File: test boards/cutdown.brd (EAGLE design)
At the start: 50.8 x 59.7 mm, 12 parts, among them Q1 FDD3706, U1 6N138M

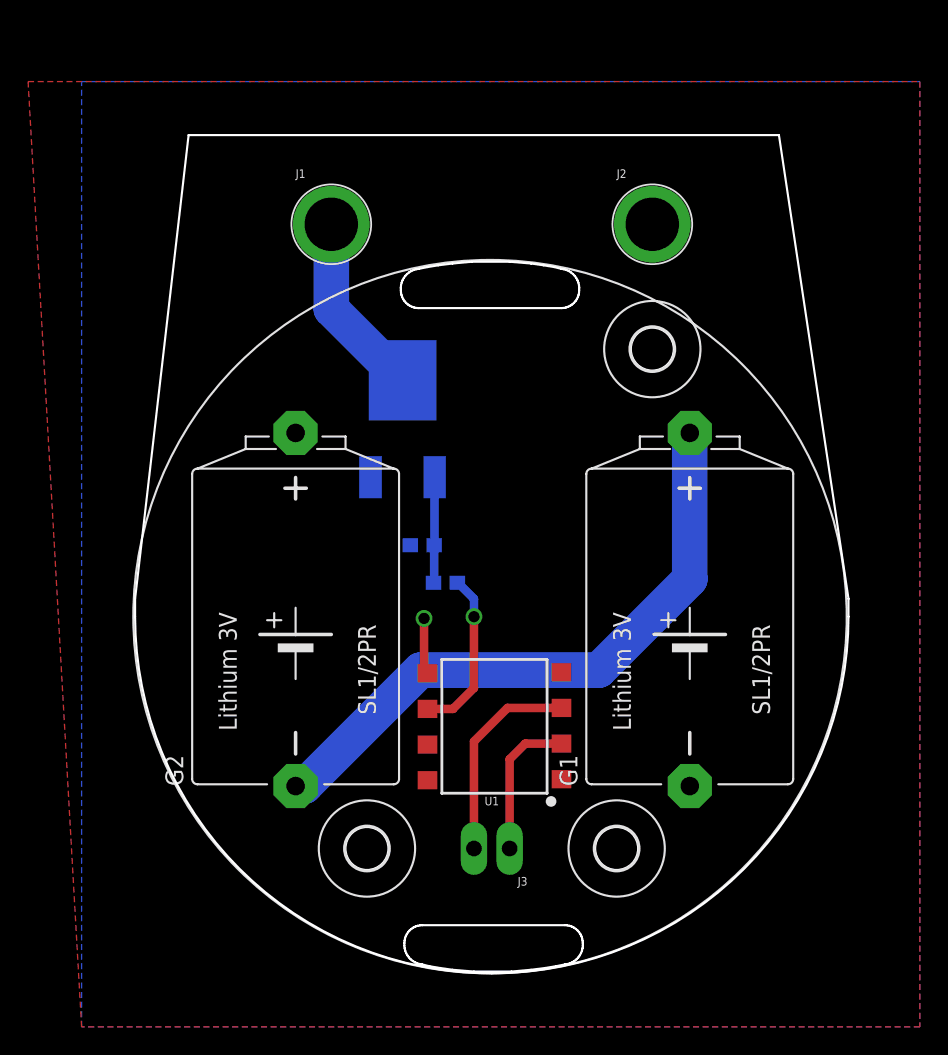
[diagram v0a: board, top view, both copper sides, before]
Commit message: updated board outline
updated board outline to makek the bottom cutout complete.
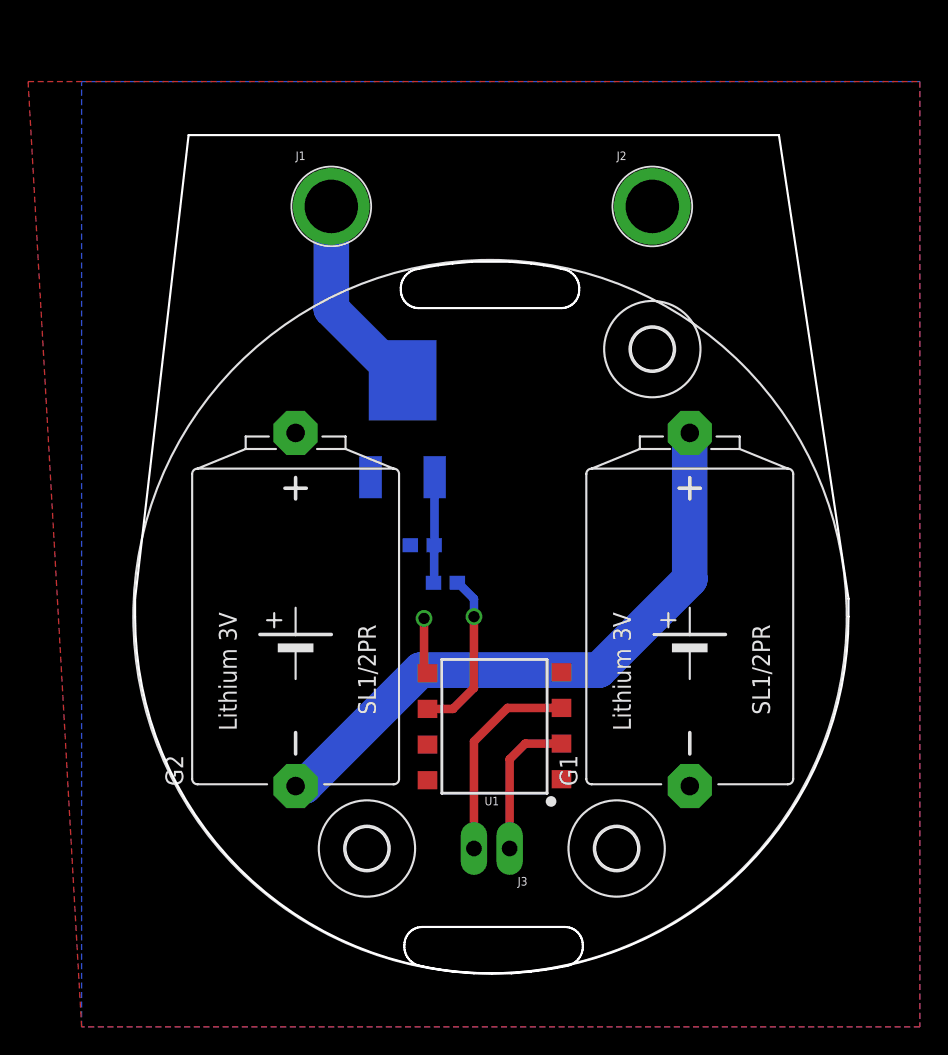
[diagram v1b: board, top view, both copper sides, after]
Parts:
- moved J1 1.27 mm to (31.8, 74.9)
- moved J2 1.27 mm to (54.6, 74.9)
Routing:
- net N$2: track 13.2 -> 14.5 mm
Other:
- outline, holes or cut-outs redrawn
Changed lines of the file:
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@@
 <wire x1="68.58" y1="46.99" x2="63.627" y2="80.01" width="0.1524" layer="20"/>
 <wire x1="17.78" y1="46.99" x2="17.78" y2="45.72" width="0.1524" layer="20"/>
-<wire x1="17.78" y1="45.72" x2="43.18" y2="20.32" width="0.1524" layer="20" curve="90"/>
-<wire x1="43.18" y1="20.32" x2="68.58" y2="45.72" width="0.1524" layer="20" curve="90"/>
+<wire x1="17.78" y1="45.72" x2="43.18" y2="20.32" width="0.1524" layer="20" curve="90" locked="yes"/>
+<wire x1="43.18" y1="20.32" x2="68.58" y2="45.72" width="0.1524" layer="20" curve="90" locked="yes"/>
 <wire x1="68.58" y1="45.72" x2="68.58" y2="46.99" width="0.1524" layer="20"/>
 <polygon width="0.1524" layer="20">
@@
 </polygon>
 <polygon width="0.1524" layer="20">
-<vertex x="49.657" y="22.479" curve="-90"/>
-<vertex x="48.387" y="20.955"/>
-<vertex x="47.752" y="20.828"/>
-<vertex x="46.99" y="20.701"/>
-<vertex x="45.974" y="20.574"/>
-<vertex x="44.577" y="20.447"/>
-<vertex x="41.91" y="20.447"/>
-<vertex x="40.386" y="20.574"/>
-<vertex x="39.497" y="20.701"/>
-<vertex x="38.735" y="20.828"/>
-<vertex x="38.227" y="20.955" curve="-90"/>
-<vertex x="36.957" y="22.479" curve="-90"/>
-<vertex x="38.227" y="23.749"/>
-<vertex x="48.387" y="23.749" curve="-90"/>
+<vertex x="49.657" y="22.352" curve="-90"/>
+<vertex x="48.387" y="20.828"/>
+<vertex x="47.752" y="20.701"/>
+<vertex x="46.99" y="20.574"/>
+<vertex x="45.974" y="20.447"/>
+<vertex x="44.577" y="20.32"/>
+<vertex x="41.91" y="20.32"/>
+<vertex x="40.386" y="20.447"/>
+<vertex x="39.497" y="20.574"/>
+<vertex x="38.735" y="20.701"/>
+<vertex x="38.227" y="20.828" curve="-90"/>
+<vertex x="36.957" y="22.352" curve="-90"/>
+<vertex x="38.227" y="23.622"/>
+<vertex x="48.387" y="23.622" curve="-90"/>
 </polygon>
 <circle x="43.053" y="45.72" radius="25.4" width="0.1524" layer="25"/>
@@
 </class>
 </classes>
-<designrules name="default">
-<description language="de">&lt;b&gt;EAGLE Design Rules&lt;/b&gt;
-&lt;p&gt;
-Die Standard-Design-Rules sind so gewählt, dass sie für
-die meisten Anwendungen passen. Sollte ihre Platine
-besondere Anforderungen haben, treffen Sie die erforderlichen
-Einstellungen hier und speichern die Design Rules unter
-einem neuen Namen ab.</description>
-<description language="en">&lt;b&gt;EAGLE Design Rules&lt;/b&gt;
-&lt;p&gt;
-The default Design Rules have been set to cover
-a wide range of applications. Your particular design
-may have different requirements, so please make the
-necessary adjustments and save your customized
-design rules under a new name.</description>
+<designrules name="MF_Standard_2_Layer">
+<description language="en">&lt;b&gt;MacroFab, INC. EAGLE Design Rules&lt;/b&gt;
+&lt;p&gt;This DRC check is for 2-Layer Standard Capability boards to be manufactured through the MacroFab, INC. service.</description>
 <param name="layerSetup" value="(1*16)"/>
-<param name="mtCopper" value="0.035mm 0.035mm 0.035mm 0.035mm 0.035mm 0.035mm 0.035mm 0.035mm 0.035mm 0.035mm 0.035mm 0.035mm 0.035mm 0.035mm 0.035mm 0.035mm"/>
-<param name="mtIsolate" value="1.5mm 0.15mm 0.2mm 0.15mm 0.2mm 0.15mm 0.2mm 0.15mm 0.2mm 0.15mm 0.2mm 0.15mm 0.2mm 0.15mm 0.2mm"/>
-<param name="mdWireWire" value="6mil"/>
-<param name="mdWirePad" value="6mil"/>
-<param name="mdWireVia" value="6mil"/>
-<param name="mdPadPad" value="6mil"/>
-<param name="mdPadVia" value="6mil"/>
-<param name="mdViaVia" value="6mil"/>
-<param name="mdSmdPad" value="6mil"/>
-<param name="mdSmdVia" value="6mil"/>
-<param name="mdSmdSmd" value="6mil"/>
-<param name="mdViaViaSameLayer" value="6mil"/>
+<param name="mtCopper" value="0.035mm 0.0175mm 0.035mm 0.035mm 0.035mm 0.035mm 0.035mm 0.035mm 0.035mm 0.035mm 0.035mm 0.035mm 0.035mm 0.035mm 0.0175mm 0.035mm"/>
+<param name="mtIsolate" value="1.5mm 1.1mm 0.2mm 0.15mm 0.2mm 0.15mm 0.2mm 0.15mm 0.2mm 0.15mm 0.2mm 0.15mm 0.2mm 0.15mm 0.2mm"/>
+<param name="mdWireWire" value="5mil"/>
+<param name="mdWirePad" value="5mil"/>
+<param name="mdWireVia" value="5mil"/>
+<param name="mdPadPad" value="5mil"/>
+<param name="mdPadVia" value="5mil"/>
+<param name="mdViaVia" value="5mil"/>
+<param name="mdSmdPad" value="0mil"/>
+<param name="mdSmdVia" value="0mil"/>
+<param name="mdSmdSmd" value="0mil"/>
+<param name="mdViaViaSameLayer" value="8mil"/>
 <param name="mnLayersViaInSmd" value="2"/>
-<param name="mdCopperDimension" value="40mil"/>
-<param name="mdDrill" value="6mil"/>
+<param name="mdCopperDimension" value="10mil"/>
+<param name="mdDrill" value="10mil"/>
 <param name="mdSmdStop" value="0mil"/>
-<param name="msWidth" value="6mil"/>
-<param name="msDrill" value="0.35mm"/>
-<param name="msMicroVia" value="9.99mm"/>
+<param name="msWidth" value="5mil"/>
+<param name="msDrill" value="12mil"/>
+<param name="msMicroVia" value="12mil"/>
 <param name="msBlindViaRatio" value="0.5"/>
 <param name="rvPadTop" value="0.25"/>
@@
 <param name="rvMicroViaOuter" value="0.25"/>
 <param name="rvMicroViaInner" value="0.25"/>
-<param name="rlMinPadTop" value="10mil"/>
+<param name="rlMinPadTop" value="6mil"/>
 <param name="rlMaxPadTop" value="20mil"/>
-<param name="rlMinPadInner" value="10mil"/>
+<param name="rlMinPadInner" value="6mil"/>
 <param name="rlMaxPadInner" value="20mil"/>
-<param name="rlMinPadBottom" value="10mil"/>
+<param name="rlMinPadBottom" value="6mil"/>
 <param name="rlMaxPadBottom" value="20mil"/>
-<param name="rlMinViaOuter" value="8mil"/>
+<param name="rlMinViaOuter" value="6mil"/>
 <param name="rlMaxViaOuter" value="20mil"/>
-<param name="rlMinViaInner" value="8mil"/>
+<param name="rlMinViaInner" value="6mil"/>
 <param name="rlMaxViaInner" value="20mil"/>
-<param name="rlMinMicroViaOuter" value="4mil"/>
+<param name="rlMinMicroViaOuter" value="6mil"/>
 <param name="rlMaxMicroViaOuter" value="20mil"/>
-<param name="rlMinMicroViaInner" value="4mil"/>
+<param name="rlMinMicroViaInner" value="6mil"/>
 <param name="rlMaxMicroViaInner" value="20mil"/>
 <param name="psTop" value="-1"/>
 <param name="psBottom" value="-1"/>
-<param name="psFirst" value="-1"/>
+<param name="psFirst" value="0"/>
 <param name="psElongationLong" value="100"/>
 <param name="psElongationOffset" value="100"/>
 <param name="mvStopFrame" value="1"/>
 <param name="mvCreamFrame" value="0"/>
-<param name="mlMinStopFrame" value="4mil"/>
-<param name="mlMaxStopFrame" value="4mil"/>
+<param name="mlMinStopFrame" value="2mil"/>
+<param name="mlMaxStopFrame" value="2mil"/>
 <param name="mlMinCreamFrame" value="0mil"/>
 <param name="mlMaxCreamFrame" value="0mil"/>
-<param name="mlViaStopLimit" value="0mil"/>
+<param name="mlViaStopLimit" value="25mil"/>
 <param name="srRoundness" value="0"/>
 <param name="srMinRoundness" value="0mil"/>
@@
 <param name="checkAngle" value="0"/>
 <param name="checkFont" value="1"/>
-<param name="checkRestrict" value="1"/>
+<param name="checkRestrict" value="0"/>
 <param name="checkStop" value="0"/>
 <param name="checkValues" value="0"/>
@@
 <attribute name="PROD_ID" value="IC-09482" x="43.18" y="38.1" size="1.778" layer="27" rot="R90" display="off"/>
 </element>
-<element name="J1" library="SparkFun-Connectors" library_urn="urn:adsk.eagle:library:513" package="BANANA_CONN" package3d_urn="urn:adsk.eagle:package:38018/1" value="" x="31.75" y="73.66"/>
-<element name="J2" library="SparkFun-Connectors" library_urn="urn:adsk.eagle:library:513" package="BANANA_CONN" package3d_urn="urn:adsk.eagle:package:38018/1" value="" x="54.61" y="73.66"/>
+<element name="J1" library="SparkFun-Connectors" library_urn="urn:adsk.eagle:library:513" package="BANANA_CONN" package3d_urn="urn:adsk.eagle:package:38018/1" value="" x="31.75" y="74.93"/>
+<element name="J2" library="SparkFun-Connectors" library_urn="urn:adsk.eagle:library:513" package="BANANA_CONN" package3d_urn="urn:adsk.eagle:package:38018/1" value="" x="54.61" y="74.93"/>
 <element name="J3" library="SparkFun-Connectors" library_urn="urn:adsk.eagle:library:513" package="1X02_LONGPADS" package3d_urn="urn:adsk.eagle:package:38048/1" value="" x="44.45" y="29.21" rot="R180"/>
 <element name="R1" library="SparkFun-Resistors" library_urn="urn:adsk.eagle:library:532" package="0603" package3d_urn="urn:adsk.eagle:package:39650/1" value="10" x="39.878" y="48.133" rot="MR0">
@@
 <contactref element="J1" pad="P$1"/>
 <contactref element="Q1" pad="4"/>
-<wire x1="31.75" y1="73.66" x2="31.75" y2="67.628" width="2.54" layer="16"/>
+<wire x1="31.75" y1="74.93" x2="31.75" y2="67.628" width="2.54" layer="16"/>
 <wire x1="31.75" y1="67.628" x2="36.83" y2="62.548" width="2.54" layer="16"/>
 </signal>
@@
 packages will not be understood (or retained) with this version.
 </note>
+<note version="8.5" severity="warning">
+Since Version 8.5, EAGLE supports locking for holes, vias, wires and polygons.
+The locking property on all objects of these types will not be understood in this version.
+</note>
 </compatibility>

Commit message: Added boards
Added boards for a cutdown circuit, spi flash storage and spi flash breakout board and a shield template.
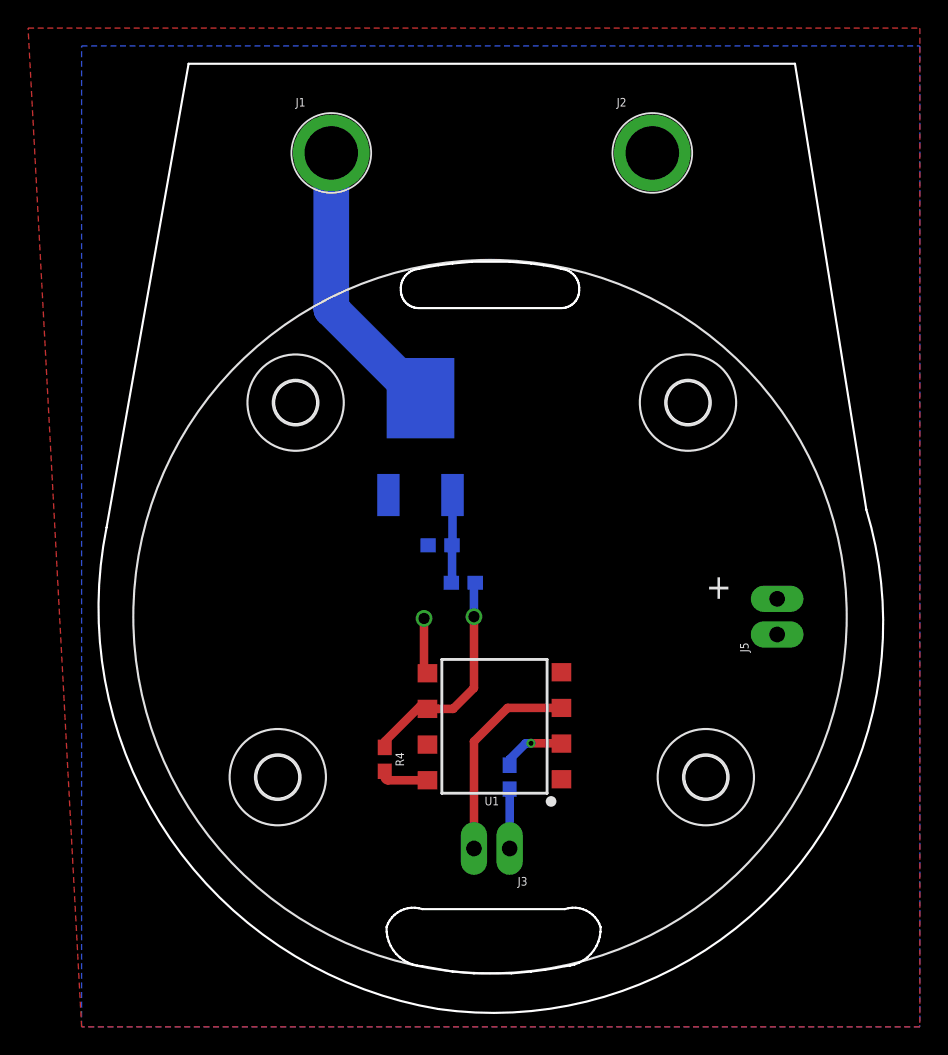
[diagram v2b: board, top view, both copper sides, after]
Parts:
- removed G1, G2: SL-150-1/2AA/PR, battery:SL-150-1/2AA/PR
- added H1: MOUNT-HOLE3.0, holes:3,0
- added J5: (no value), SparkFun-Connectors:1X02_LONGPADS
- added R3: 330, SparkFun-Resistors:0603
- added R4: 2.2k, SparkFun-Resistors:0603
- moved H4 8.13 mm to (58.4, 34.3)
- moved H3 8.13 mm to (27.9, 34.3)
- moved H6 4.58 mm to (57.1, 61.0)
- moved J1 3.81 mm to (31.8, 78.7)
- moved J2 3.81 mm to (54.6, 78.7)
- moved Q1 1.80 mm to (38.1, 59.7)
- moved R1 1.27 mm to (41.1, 48.1)
- moved R2 1.27 mm to (39.5, 50.8)
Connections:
- removed net N$1: G1.+, G2.-
- new net N$5: R3.2, U1.2
- new net N$6: R4.2, U1.8
- net A: now also R3.1; no longer U1.2
- net GND: now also J5.1; no longer G1.-
- net N$4: now also R4.1
- net VCC: now also J5.2; no longer G2.+, U1.8
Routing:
- net N$1: track 44.6 -> 0.00 mm
- net A: track 10.5 -> 4.23 mm
- net N$2: track 14.5 -> 20.1 mm
- net N$5: track 0.00 -> 4.59 mm, vias 0 -> 1
- net N$4: track 12.2 -> 16.3 mm
- net N$6: track 0.00 -> 3.13 mm
- net N$3: track 7.55 -> 6.28 mm
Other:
- board size 50.8 x 59.7 mm -> 55.9 x 67.6 mm
- board text added: "+"
